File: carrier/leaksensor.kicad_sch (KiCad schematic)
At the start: 24 parts, among them SW1 KEYSW, SW2 KEYSW, SW3 KEYSW, SW4 KEYSW, SW5 KEYSW, SW6 KEYSW, SW7 KEYSW, SW8 KEYSW, SW9 KEYSW

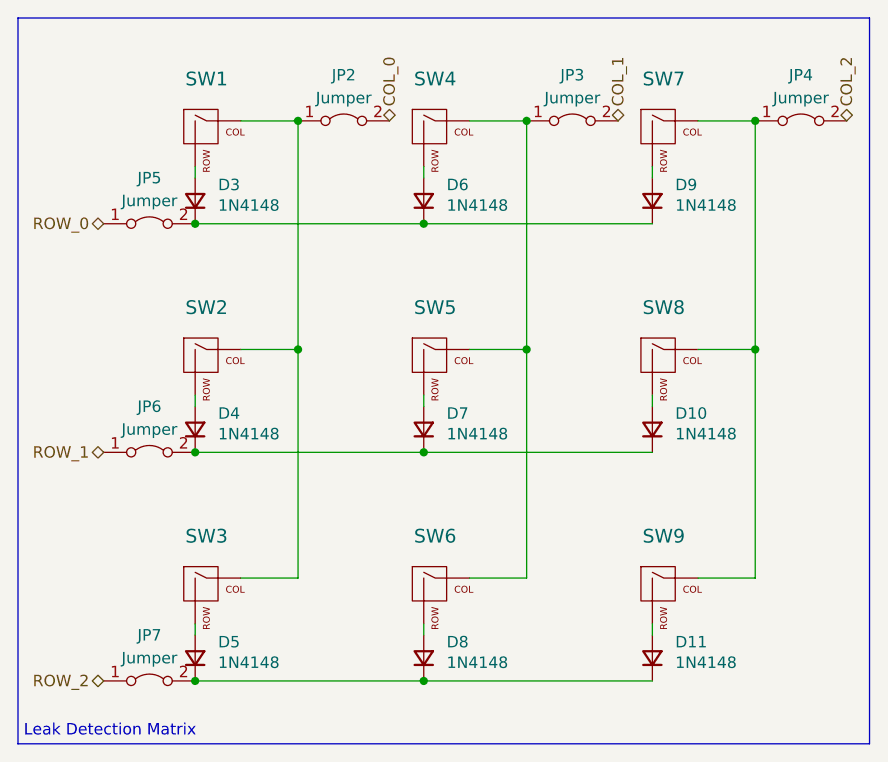
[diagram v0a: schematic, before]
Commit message: Refactor: small changes for carrier, cm4 and leaksensors
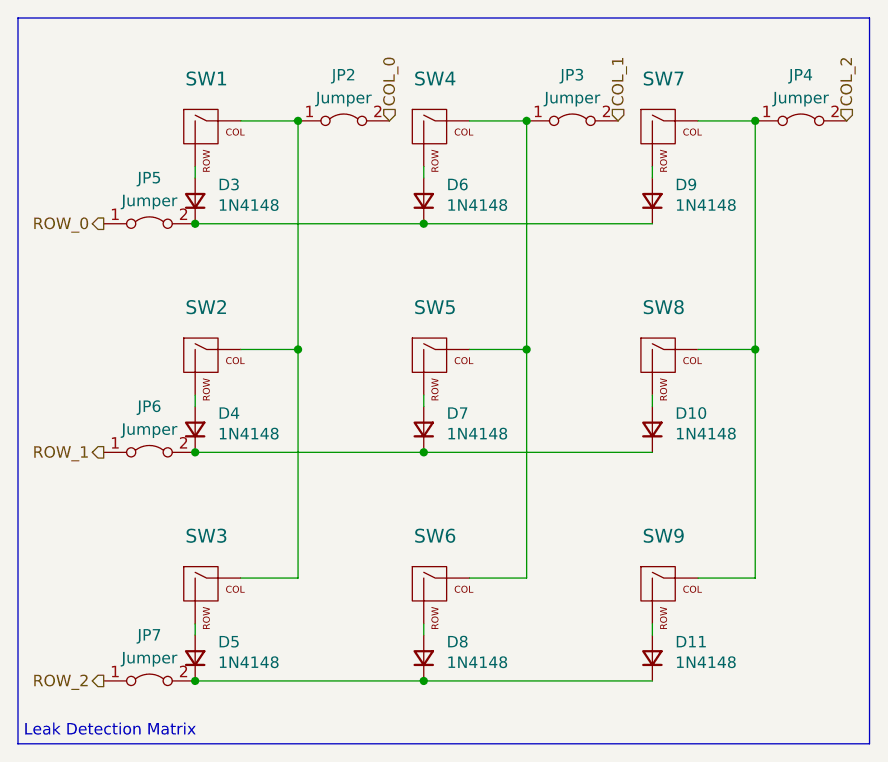
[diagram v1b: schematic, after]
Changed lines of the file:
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@@
     (effects (font (size 1.27 1.27)) (justify left bottom))
   )
-  (hierarchical_label "ROW_2" (shape bidirectional) (at 86.36 128.27 180) (fields_autoplaced)
+  (hierarchical_label "ROW_2" (shape output) (at 86.36 128.27 180) (fields_autoplaced)
     (effects (font (size 1.27 1.27)) (justify right))
   )
-  (hierarchical_label "ROW_0" (shape bidirectional) (at 86.36 77.47 180) (fields_autoplaced)
+  (hierarchical_label "ROW_0" (shape output) (at 86.36 77.47 180) (fields_autoplaced)
     (effects (font (size 1.27 1.27)) (justify right))
   )
-  (hierarchical_label "COL_1" (shape bidirectional) (at 143.51 66.04 90) (fields_autoplaced)
+  (hierarchical_label "COL_1" (shape input) (at 143.51 66.04 90) (fields_autoplaced)
     (effects (font (size 1.27 1.27)) (justify left))
   )
-  (hierarchical_label "COL_0" (shape bidirectional) (at 118.11 66.04 90) (fields_autoplaced)
+  (hierarchical_label "COL_0" (shape input) (at 118.11 66.04 90) (fields_autoplaced)
     (effects (font (size 1.27 1.27)) (justify left))
   )
-  (hierarchical_label "COL_2" (shape bidirectional) (at 168.91 66.04 90) (fields_autoplaced)
+  (hierarchical_label "COL_2" (shape input) (at 168.91 66.04 90) (fields_autoplaced)
     (effects (font (size 1.27 1.27)) (justify left))
   )
-  (hierarchical_label "ROW_1" (shape bidirectional) (at 86.36 102.87 180) (fields_autoplaced)
+  (hierarchical_label "ROW_1" (shape output) (at 86.36 102.87 180) (fields_autoplaced)
     (effects (font (size 1.27 1.27)) (justify right))
   )

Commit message: Fix: relinked footprints
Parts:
- JP2, JP3, JP4, JP5, JP6, JP7: footprint (none) -> Jumper:SolderJumper-2_P1.3mm_Bridged_Pad1.0x1.5mm
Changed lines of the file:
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@@
       (effects (font (size 1.27 1.27)))
     )
-    (property "Footprint" "" (at 163.83 66.04 0)
+    (property "Footprint" "Jumper:SolderJumper-2_P1.3mm_Bridged_Pad1.0x1.5mm" (at 163.83 66.04 0)
       (effects (font (size 1.27 1.27)) hide)
     )
@@
       (effects (font (size 1.27 1.27)))
     )
-    (property "Footprint" "" (at 91.44 102.87 0)
+    (property "Footprint" "Jumper:SolderJumper-2_P1.3mm_Bridged_Pad1.0x1.5mm" (at 91.44 102.87 0)
       (effects (font (size 1.27 1.27)) hide)
     )
@@
       (effects (font (size 1.27 1.27)))
     )
-    (property "Footprint" "" (at 91.44 77.47 0)
+    (property "Footprint" "Jumper:SolderJumper-2_P1.3mm_Bridged_Pad1.0x1.5mm" (at 91.44 77.47 0)
       (effects (font (size 1.27 1.27)) hide)
     )
@@
       (effects (font (size 1.27 1.27)))
     )
-    (property "Footprint" "" (at 113.03 66.04 0)
+    (property "Footprint" "Jumper:SolderJumper-2_P1.3mm_Bridged_Pad1.0x1.5mm" (at 113.03 66.04 0)
       (effects (font (size 1.27 1.27)) hide)
     )
@@
       (effects (font (size 1.27 1.27)))
     )
-    (property "Footprint" "" (at 138.43 66.04 0)
+    (property "Footprint" "Jumper:SolderJumper-2_P1.3mm_Bridged_Pad1.0x1.5mm" (at 138.43 66.04 0)
       (effects (font (size 1.27 1.27)) hide)
     )
@@
       (effects (font (size 1.27 1.27)))
     )
-    (property "Footprint" "" (at 91.44 128.27 0)
-      (effects (font (size 1.27 1.27)) hide)
-    )
+    (property "Footprint" "Jumper:SolderJumper-2_P1.3mm_Bridged_Pad1.0x1.5mm" (at 91.44 128.27 0)
+      (effects (font (size 1.27 1.27)) hide)
+    )

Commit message: Feat: begun work on carrier pcb and imported NGFF m.2 library
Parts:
- D10, D11, D3, D4, D5, D6, D7, D8, D9: footprint Diode_THT:D_DO-35_SOD27_P7.62mm_Horizontal -> Diode_SMD:D_0603_1608Metric
- SW1, SW2, SW3, SW4, SW5, SW6, SW7, SW8, SW9: footprint Button_Switch_Keyboard:SW_Cherry_MX_1.00u_PCB -> Connector_JST:JST_GH_BM02B-GHS-TBT_1x02-1MP_P1.25mm_Vertical
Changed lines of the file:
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@@
       (effects (font (face "Fira Code") (size 1.27 1.27)) (justify right))
     )
-    (property "Footprint" "Diode_THT:D_DO-35_SOD27_P7.62mm_Horizontal" (at 123.19 82.55 0)
+    (property "Footprint" "Diode_SMD:D_0603_1608Metric" (at 123.19 82.55 0)
       (effects (font (face "Fira Code") (size 1.27 1.27)) hide)
     )
@@
       (effects (font (face "Fira Code") (size 1.27 1.27)) (justify right))
     )
-    (property "Footprint" "Diode_THT:D_DO-35_SOD27_P7.62mm_Horizontal" (at 148.59 107.95 0)
+    (property "Footprint" "Diode_SMD:D_0603_1608Metric" (at 148.59 107.95 0)
       (effects (font (face "Fira Code") (size 1.27 1.27)) hide)
     )
@@
       (effects (font (face "Fira Code") (size 1.524 1.524)) hide)
     )
-    (property "Footprint" "Button_Switch_Keyboard:SW_Cherry_MX_1.00u_PCB" (at 97.79 67.31 0)
+    (property "Footprint" "Connector_JST:JST_GH_BM02B-GHS-TBT_1x02-1MP_P1.25mm_Vertical" (at 97.79 67.31 0)
       (effects (font (face "Fira Code") (size 1.524 1.524)) hide)
     )
@@
       (effects (font (face "Fira Code") (size 1.524 1.524)) hide)
     )
-    (property "Footprint" "Button_Switch_Keyboard:SW_Cherry_MX_1.00u_PCB" (at 148.59 67.31 0)
+    (property "Footprint" "Connector_JST:JST_GH_BM02B-GHS-TBT_1x02-1MP_P1.25mm_Vertical" (at 148.59 67.31 0)
       (effects (font (face "Fira Code") (size 1.524 1.524)) hide)
     )
@@
       (effects (font (face "Fira Code") (size 1.524 1.524)) hide)
     )
-    (property "Footprint" "Button_Switch_Keyboard:SW_Cherry_MX_1.00u_PCB" (at 123.19 118.11 0)
+    (property "Footprint" "Connector_JST:JST_GH_BM02B-GHS-TBT_1x02-1MP_P1.25mm_Vertical" (at 123.19 118.11 0)
       (effects (font (face "Fira Code") (size 1.524 1.524)) hide)
     )
@@
       (effects (font (face "Fira Code") (size 1.524 1.524)) hide)
     )
-    (property "Footprint" "Button_Switch_Keyboard:SW_Cherry_MX_1.00u_PCB" (at 97.79 92.71 0)
+    (property "Footprint" "Connector_JST:JST_GH_BM02B-GHS-TBT_1x02-1MP_P1.25mm_Vertical" (at 97.79 92.71 0)
       (effects (font (face "Fira Code") (size 1.524 1.524)) hide)
     )
@@
       (effects (font (face "Fira Code") (size 1.27 1.27)) (justify right))
     )
-    (property "Footprint" "Diode_THT:D_DO-35_SOD27_P7.62mm_Horizontal" (at 123.19 107.95 0)
+    (property "Footprint" "Diode_SMD:D_0603_1608Metric" (at 123.19 107.95 0)
       (effects (font (face "Fira Code") (size 1.27 1.27)) hide)
     )
@@
       (effects (font (face "Fira Code") (size 1.524 1.524)) hide)
     )
-    (property "Footprint" "Button_Switch_Keyboard:SW_Cherry_MX_1.00u_PCB" (at 123.19 67.31 0)
+    (property "Footprint" "Connector_JST:JST_GH_BM02B-GHS-TBT_1x02-1MP_P1.25mm_Vertical" (at 123.19 67.31 0)
       (effects (font (face "Fira Code") (size 1.524 1.524)) hide)
     )
@@
       (effects (font (face "Fira Code") (size 1.27 1.27)) (justify right))
     )
-    (property "Footprint" "Diode_THT:D_DO-35_SOD27_P7.62mm_Horizontal" (at 148.59 133.35 0)
+    (property "Footprint" "Diode_SMD:D_0603_1608Metric" (at 148.59 133.35 0)
       (effects (font (face "Fira Code") (size 1.27 1.27)) hide)
     )
@@
       (effects (font (face "Fira Code") (size 1.27 1.27)) (justify right))
     )
-    (property "Footprint" "Diode_THT:D_DO-35_SOD27_P7.62mm_Horizontal" (at 97.79 82.55 0)
+    (property "Footprint" "Diode_SMD:D_0603_1608Metric" (at 97.79 82.55 0)
       (effects (font (face "Fira Code") (size 1.27 1.27)) hide)
     )
@@
       (effects (font (face "Fira Code") (size 1.524 1.524)) hide)
     )
-    (property "Footprint" "Button_Switch_Keyboard:SW_Cherry_MX_1.00u_PCB" (at 97.79 118.11 0)
+    (property "Footprint" "Connector_JST:JST_GH_BM02B-GHS-TBT_1x02-1MP_P1.25mm_Vertical" (at 97.79 118.11 0)
       (effects (font (face "Fira Code") (size 1.524 1.524)) hide)
     )
@@
       (effects (font (face "Fira Code") (size 1.524 1.524)) hide)
     )
-    (property "Footprint" "Button_Switch_Keyboard:SW_Cherry_MX_1.00u_PCB" (at 148.59 118.11 0)
+    (property "Footprint" "Connector_JST:JST_GH_BM02B-GHS-TBT_1x02-1MP_P1.25mm_Vertical" (at 148.59 118.11 0)
       (effects (font (face "Fira Code") (size 1.524 1.524)) hide)
     )
@@
       (effects (font (face "Fira Code") (size 1.524 1.524)) hide)
     )
-    (property "Footprint" "Button_Switch_Keyboard:SW_Cherry_MX_1.00u_PCB" (at 148.59 92.71 0)
+    (property "Footprint" "Connector_JST:JST_GH_BM02B-GHS-TBT_1x02-1MP_P1.25mm_Vertical" (at 148.59 92.71 0)
       (effects (font (face "Fira Code") (size 1.524 1.524)) hide)
     )
@@
       (effects (font (face "Fira Code") (size 1.27 1.27)) (justify right))
     )
-    (property "Footprint" "Diode_THT:D_DO-35_SOD27_P7.62mm_Horizontal" (at 123.19 133.35 0)
+    (property "Footprint" "Diode_SMD:D_0603_1608Metric" (at 123.19 133.35 0)
       (effects (font (face "Fira Code") (size 1.27 1.27)) hide)
     )
@@
       (effects (font (face "Fira Code") (size 1.27 1.27)) (justify right))
     )
-    (property "Footprint" "Diode_THT:D_DO-35_SOD27_P7.62mm_Horizontal" (at 97.79 133.35 0)
+    (property "Footprint" "Diode_SMD:D_0603_1608Metric" (at 97.79 133.35 0)
       (effects (font (face "Fira Code") (size 1.27 1.27)) hide)
     )
@@
       (effects (font (face "Fira Code") (size 1.27 1.27)) (justify right))
     )
-    (property "Footprint" "Diode_THT:D_DO-35_SOD27_P7.62mm_Horizontal" (at 148.59 82.55 0)
+    (property "Footprint" "Diode_SMD:D_0603_1608Metric" (at 148.59 82.55 0)
       (effects (font (face "Fira Code") (size 1.27 1.27)) hide)
     )
@@
       (effects (font (face "Fira Code") (size 1.27 1.27)) (justify right))
     )
-    (property "Footprint" "Diode_THT:D_DO-35_SOD27_P7.62mm_Horizontal" (at 97.79 107.95 0)
+    (property "Footprint" "Diode_SMD:D_0603_1608Metric" (at 97.79 107.95 0)
       (effects (font (face "Fira Code") (size 1.27 1.27)) hide)
     )
@@
       (effects (font (face "Fira Code") (size 1.524 1.524)) hide)
     )
-    (property "Footprint" "Button_Switch_Keyboard:SW_Cherry_MX_1.00u_PCB" (at 123.19 92.71 0)
-      (effects (font (face "Fira Code") (size 1.524 1.524)) hide)
-    )
+    (property "Footprint" "Connector_JST:JST_GH_BM02B-GHS-TBT_1x02-1MP_P1.25mm_Vertical" (at 123.19 92.71 0)
+      (effects (font (face "Fira Code") (size 1.524 1.524)) hide)
+    )

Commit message: feat: carrier board layout v2
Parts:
- removed D10, D11, D5, D8, D9: 1N4148, Diode_SMD:D_0603_1608Metric, symbol Device:D_Small
- removed JP4, JP7: Jumper, Jumper:SolderJumper-2_P1.3mm_Bridged_Pad1.0x1.5mm, symbol Jumper:Jumper_2_Bridged
- removed SW3, SW6, SW7, SW8, SW9: KEYSW, Connector_JST:JST_GH_BM02B-GHS-TBT_1x02-1MP_P1.25mm_Vertical, symbol MX_Alps_Hybrid:MX-NoLED
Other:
- moved on the sheet: D3, D4, D6, D7, JP2, JP3, JP5, JP6, SW1, SW2, SW4, SW5

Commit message: Feat: restructured lower half to fit ADC + power LEDs
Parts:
- D3, D4, D6, D7: footprint Diode_SMD:D_0603_1608Metric -> Diode_SMD:D_SOD-323
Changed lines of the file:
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@@
       (effects (font (face "Fira Code") (size 1.27 1.27)) (justify right))
     )
-    (property "Footprint" "Diode_SMD:D_0603_1608Metric" (at 134.62 92.71 0)
+    (property "Footprint" "Diode_SMD:D_SOD-323" (at 134.62 92.71 0)
       (effects (font (face "Fira Code") (size 1.27 1.27)) hide)
     )
@@
       (effects (font (face "Fira Code") (size 1.27 1.27)) (justify right))
     )
-    (property "Footprint" "Diode_SMD:D_0603_1608Metric" (at 134.62 118.11 0)
+    (property "Footprint" "Diode_SMD:D_SOD-323" (at 134.62 118.11 0)
       (effects (font (face "Fira Code") (size 1.27 1.27)) hide)
     )
@@
       (effects (font (face "Fira Code") (size 1.27 1.27)) (justify right))
     )
-    (property "Footprint" "Diode_SMD:D_0603_1608Metric" (at 109.22 92.71 0)
+    (property "Footprint" "Diode_SMD:D_SOD-323" (at 109.22 92.71 0)
       (effects (font (face "Fira Code") (size 1.27 1.27)) hide)
     )
@@
       (effects (font (face "Fira Code") (size 1.27 1.27)) (justify right))
     )
-    (property "Footprint" "Diode_SMD:D_0603_1608Metric" (at 109.22 118.11 0)
-      (effects (font (face "Fira Code") (size 1.27 1.27)) hide)
-    )
+    (property "Footprint" "Diode_SMD:D_SOD-323" (at 109.22 118.11 0)
+      (effects (font (face "Fira Code") (size 1.27 1.27)) hide)
+    )
